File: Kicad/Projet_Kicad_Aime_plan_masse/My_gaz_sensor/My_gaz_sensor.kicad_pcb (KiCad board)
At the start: 2 copper layers, 134.6 x 64.8 mm, 23 parts, among them J1 Conn_01x03, J2 Conn_01x03, P1 Power, P2 Analog, P3 Digital, P4 Digital, P5 CONN_01X01, P6 CONN_01X01, P7 CONN_01X01, P8 CONN_01X01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

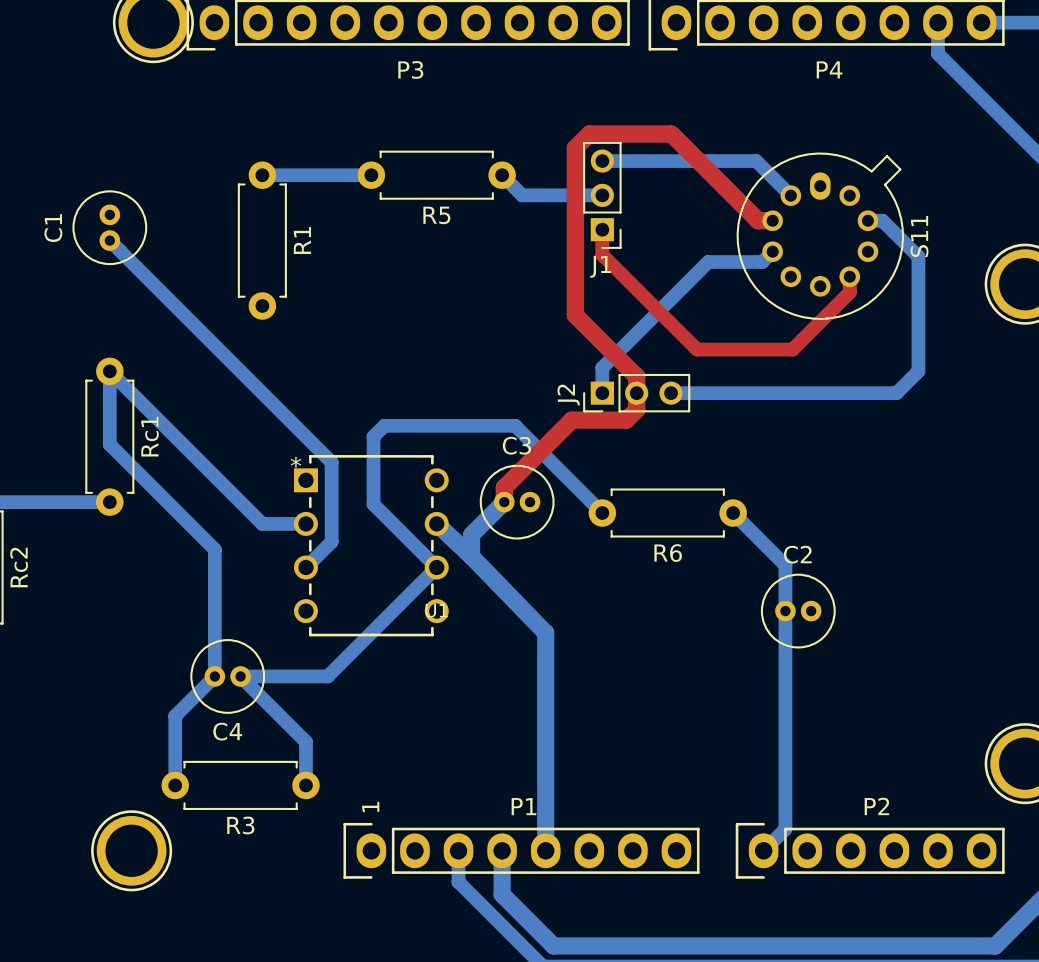
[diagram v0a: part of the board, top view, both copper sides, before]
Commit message: Refactor valeur C4
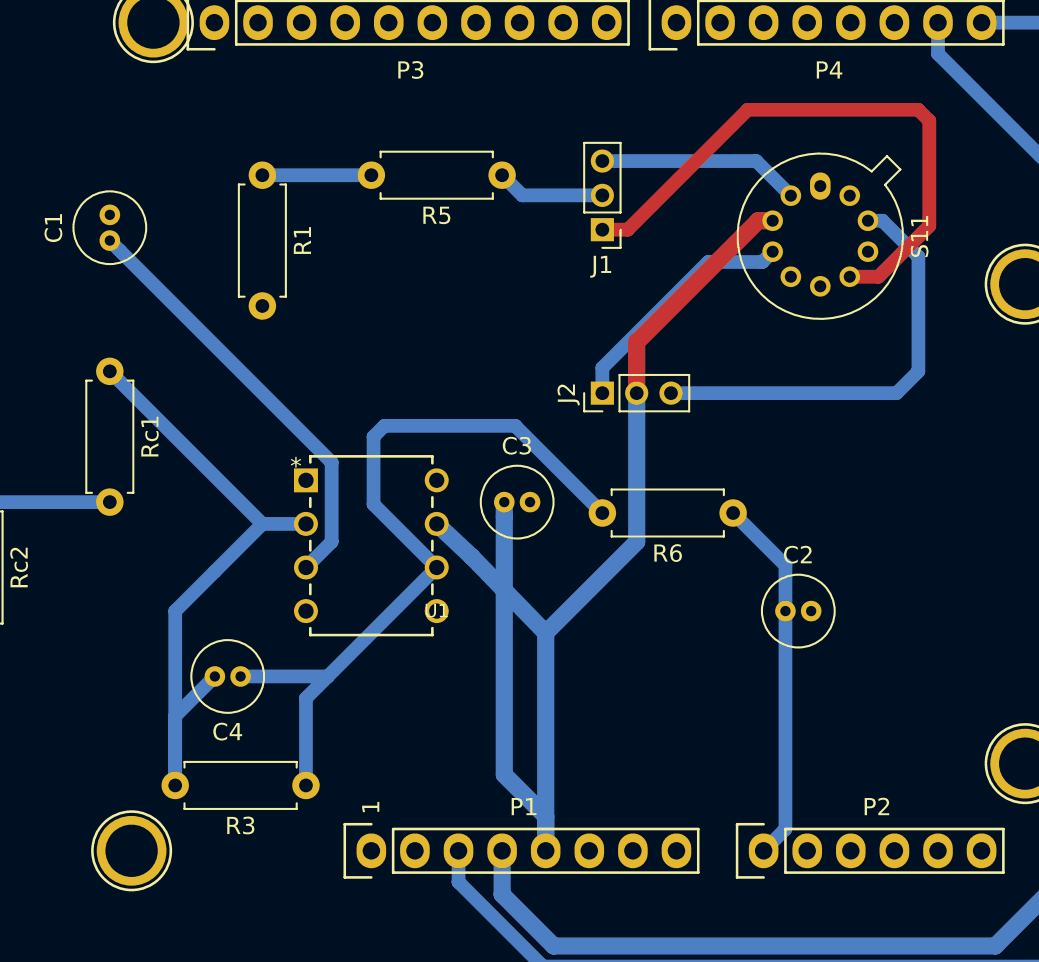
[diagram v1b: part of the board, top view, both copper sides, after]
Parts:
- C4: value 100n -> 1µ
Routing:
- net /GazSensorRight1: track 20.5 -> 34.2 mm
- net +5V: track 66.7 -> 73.0 mm
- net Net-(C4-Pad2): track 42.7 -> 39.8 mm
- net Net-(C4-Pad1): track 46.8 -> 45.8 mm
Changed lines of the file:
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@@
     (thickness 1.6)
     (drawings 25)
-    (tracks 90)
+    (tracks 84)
     (zones 0)
     (modules 23)
@@
       (effects (font (size 1 1) (thickness 0.15)))
     )
-    (fp_text value 100n (at 0.75 3.25) (layer F.Fab)
+    (fp_text value 1µ (at 0.75 3.25) (layer F.Fab)
       (effects (font (size 1 1) (thickness 0.15)))
     )
@@
   (segment (start 135.128 107.315) (end 136.626501 105.816499) (width 0.8) (layer B.Cu) (net 31))
   (segment (start 138.938 84.455) (end 132.588 84.455) (width 0.8) (layer B.Cu) (net 31))
-  (segment (start 135.128 120.015) (end 135.128 117.475) (width 0.8) (layer B.Cu) (net 32))
-  (segment (start 135.128 117.475) (end 131.318 113.665) (width 0.8) (layer B.Cu) (net 32))
   (segment (start 136.398 113.665) (end 142.748 107.315) (width 0.8) (layer B.Cu) (net 32))
   (segment (start 131.318 113.665) (end 136.398 113.665) (width 0.8) (layer B.Cu) (net 32))
@@
   (segment (start 139.7 99.06) (end 139.065 99.695) (width 0.8) (layer B.Cu) (net 32))
   (segment (start 147.32 99.06) (end 139.7 99.06) (width 0.8) (layer B.Cu) (net 32))
+  (segment (start 135.128 114.935) (end 136.398 113.665) (width 0.8) (layer B.Cu) (net 32))
+  (segment (start 135.128 120.015) (end 135.128 114.935) (width 0.8) (layer B.Cu) (net 32))
   (segment (start 132.588 104.775) (end 123.698 95.885) (width 0.8) (layer B.Cu) (net 33))
   (segment (start 135.128 104.775) (end 132.588 104.775) (width 0.8) (layer B.Cu) (net 33))
+  (segment (start 129.818 107.545) (end 132.588 104.775) (width 0.8) (layer B.Cu) (net 33))
+  (segment (start 127.508 109.855) (end 129.818 107.545) (width 0.8) (layer B.Cu) (net 33))
+  (segment (start 127.508 120.015) (end 127.508 109.855) (width 0.8) (layer B.Cu) (net 33))
   (segment (start 127.508 115.975) (end 129.818 113.665) (width 0.8) (layer B.Cu) (net 33))
   (segment (start 127.508 120.015) (end 127.508 115.975) (width 0.8) (layer B.Cu) (net 33))
-  (segment (start 129.818 113.665) (end 129.818 106.275) (width 0.8) (layer B.Cu) (net 33))
-  (segment (start 123.698 100.155) (end 123.698 95.885) (width 0.8) (layer B.Cu) (net 33))
-  (segment (start 129.818 106.275) (end 123.698 100.155) (width 0.8) (layer B.Cu) (net 33))
   (segment (start 116.078 103.505) (end 123.698 103.505) (width 0.8) (layer B.Cu) (net 36))
   (segment (start 149.098 123.825) (end 149.098 111.125) (width 1) (layer B.Cu) (net 44))
   (segment (start 149.098 111.125) (end 144.78 106.68) (width 1) (layer B.Cu) (net 44))
   (segment (start 144.78 106.68) (end 142.748 104.775) (width 1) (layer B.Cu) (net 44))
-  (segment (start 144.78 105.41) (end 146.685 103.505) (width 1) (layer B.Cu) (net 44))
-  (segment (start 144.78 106.68) (end 144.78 105.41) (width 1) (layer B.Cu) (net 44))
-  (segment (start 154.4 98.109594) (end 154.4 97.155) (width 1) (layer F.Cu) (net 44))
-  (segment (start 153.795001 98.730001) (end 154.4 98.125002) (width 1) (layer F.Cu) (net 44))
-  (segment (start 150.611471 98.730001) (end 153.795001 98.730001) (width 1) (layer F.Cu) (net 44))
-  (segment (start 146.685 102.656472) (end 150.611471 98.730001) (width 1) (layer F.Cu) (net 44))
-  (segment (start 154.4 98.125002) (end 154.4 98.109594) (width 1) (layer F.Cu) (net 44))
-  (segment (start 146.685 103.505) (end 146.685 102.656472) (width 1) (layer F.Cu) (net 44))
-  (segment (start 154.4 96.184998) (end 154.4 96.200406) (width 1) (layer F.Cu) (net 44))
-  (segment (start 150.824999 92.609997) (end 154.4 96.184998) (width 1) (layer F.Cu) (net 44))
-  (segment (start 151.643999 82.054999) (end 150.824999 82.873999) (width 1) (layer F.Cu) (net 44))
-  (segment (start 156.421716 82.054999) (end 151.643999 82.054999) (width 1) (layer F.Cu) (net 44))
-  (segment (start 150.824999 82.873999) (end 150.824999 92.609997) (width 1) (layer F.Cu) (net 44))
-  (segment (start 161.474387 87.10767) (end 156.421716 82.054999) (width 1) (layer F.Cu) (net 44))
-  (segment (start 154.4 96.200406) (end 154.4 97.155) (width 1) (layer F.Cu) (net 44))
-  (segment (start 162.322915 87.10767) (end 161.474387 87.10767) (width 1) (layer F.Cu) (net 44))
+  (segment (start 146.685 104.353528) (end 146.685 103.505) (width 1) (layer B.Cu) (net 44))
+  (segment (start 146.685 119.396) (end 146.685 104.353528) (width 1) (layer B.Cu) (net 44))
+  (segment (start 149.098 121.809) (end 146.685 119.396) (width 1) (layer B.Cu) (net 44))
+  (segment (start 149.098 123.825) (end 149.098 121.809) (width 1) (layer B.Cu) (net 44))
+  (segment (start 161.474387 87.10767) (end 162.322915 87.10767) (width 1) (layer F.Cu) (net 44))
+  (segment (start 154.4 97.155) (end 154.4 94.182057) (width 1) (layer F.Cu) (net 44))
+  (segment (start 154.4 94.182057) (end 161.474387 87.10767) (width 1) (layer F.Cu) (net 44))
+  (segment (start 154.4 105.823) (end 154.4 97.155) (width 1) (layer B.Cu) (net 44))
+  (segment (start 149.098 111.125) (end 154.4 105.823) (width 1) (layer B.Cu) (net 44))
   (segment (start 147.733 85.63) (end 146.558 84.455) (width 0.8) (layer B.Cu) (net 45))
   (segment (start 152.4 85.63) (end 147.733 85.63) (width 0.8) (layer B.Cu) (net 45))
@@
   (segment (start 169.545 97.155) (end 156.4 97.155) (width 0.8) (layer B.Cu) (net 46))
   (segment (start 170.815 95.885) (end 169.545 97.155) (width 0.8) (layer B.Cu) (net 46))
-  (segment (start 152.4 89.105) (end 157.91 94.615) (width 0.8) (layer F.Cu) (net 47))
-  (segment (start 152.4 87.63) (end 152.4 89.105) (width 0.8) (layer F.Cu) (net 47))
-  (segment (start 166.816333 91.220858) (end 166.816333 90.37233) (width 0.8) (layer F.Cu) (net 47))
-  (segment (start 166.816333 91.285669) (end 166.816333 91.220858) (width 0.8) (layer F.Cu) (net 47))
-  (segment (start 163.487002 94.615) (end 166.816333 91.285669) (width 0.8) (layer F.Cu) (net 47))
-  (segment (start 157.91 94.615) (end 163.487002 94.615) (width 0.8) (layer F.Cu) (net 47))
+  (segment (start 168.489087 90.37233) (end 171.45 87.411417) (width 0.8) (layer F.Cu) (net 47))
+  (segment (start 166.816333 90.37233) (end 168.489087 90.37233) (width 0.8) (layer F.Cu) (net 47))
+  (segment (start 171.45 87.411417) (end 171.45 81.28) (width 0.8) (layer F.Cu) (net 47))
+  (segment (start 171.45 81.28) (end 170.815 80.645) (width 0.8) (layer F.Cu) (net 47))
+  (segment (start 153.875 87.63) (end 152.4 87.63) (width 0.8) (layer F.Cu) (net 47))
+  (segment (start 160.86 80.645) (end 153.875 87.63) (width 0.8) (layer F.Cu) (net 47))
+  (segment (start 170.815 80.645) (end 160.86 80.645) (width 0.8) (layer F.Cu) (net 47))
   (segment (start 152.4 95.68) (end 152.4 97.155) (width 0.8) (layer B.Cu) (net 49))
   (segment (start 158.567671 89.512329) (end 152.4 95.68) (width 0.8) (layer B.Cu) (net 49))

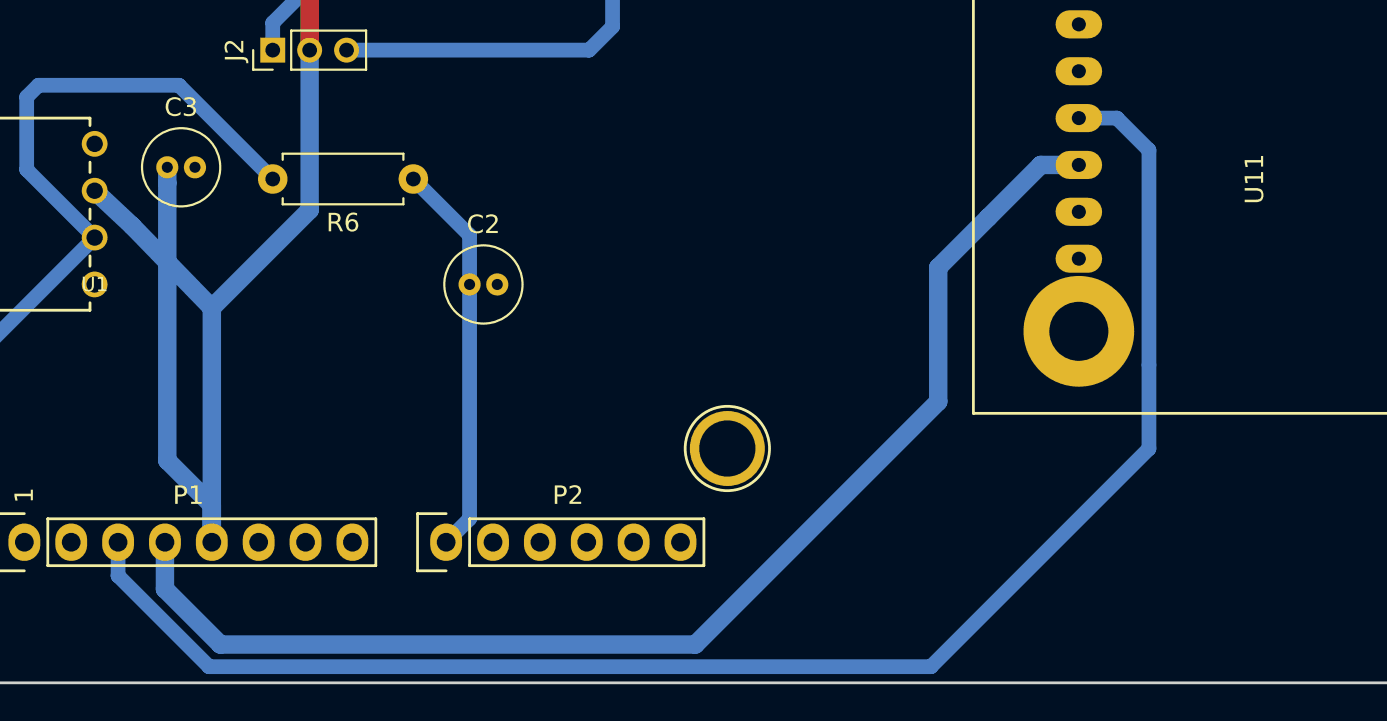
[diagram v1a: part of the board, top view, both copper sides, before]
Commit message: Reduction des near-to-pad
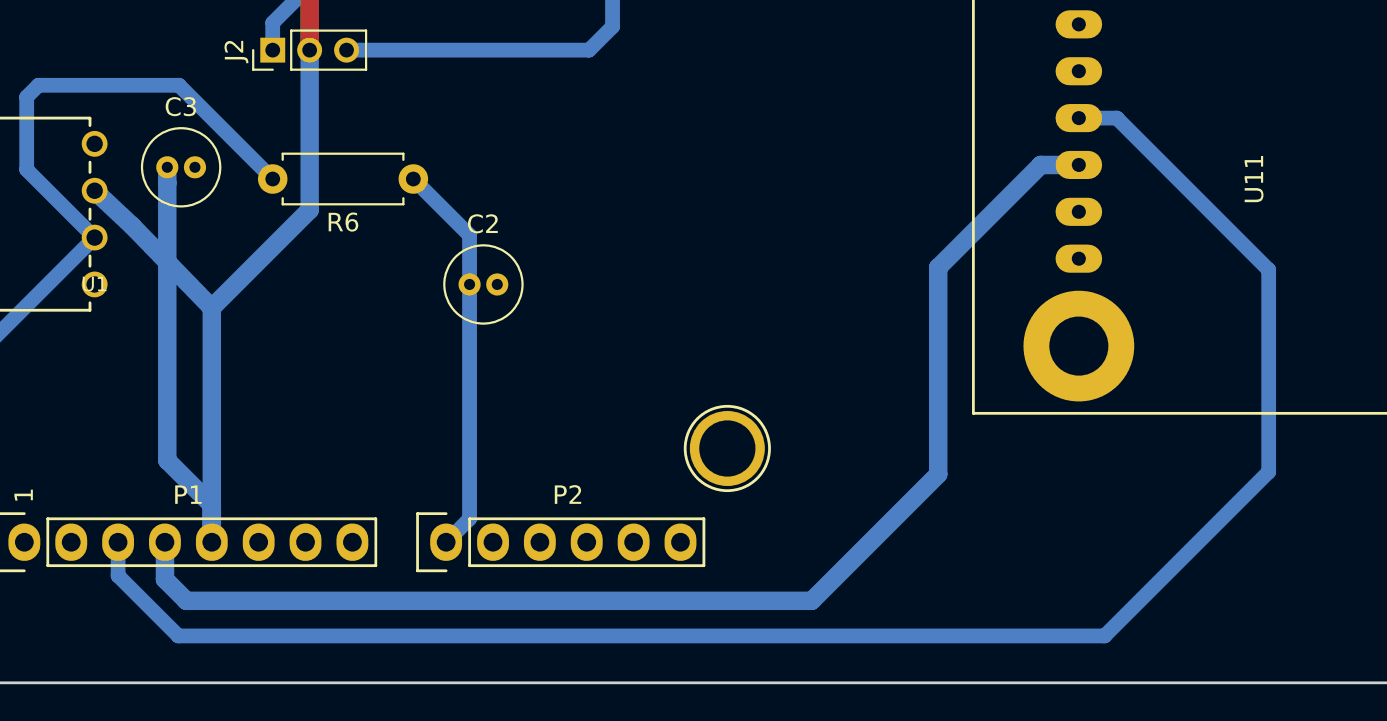
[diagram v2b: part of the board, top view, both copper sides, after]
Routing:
- net /Reset: track 85.3 -> 93.9 mm

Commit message: Changement pour s'adapter à la datasheet
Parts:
- added R7: R, Resistor_THT:R_Axial_DIN0207_L6.3mm_D2.5mm_P7.62mm_Horizontal, F.Cu at (170.8, 111.8)
- moved J2 33.8 mm to (186.1, 100.3), turned to 180 degrees
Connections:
- J2 pad 2: +5V -> +3V3
- P2 pad 2: /A1 -> SensorTemp
- S11 pad 3: +5V -> +12V
- S11 pad 6: Net-(S11-Pad6) -> SensorTemp
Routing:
- net SensorTemp: track 0.00 -> 37.9 mm
- net +5V: track 73.0 -> 43.0 mm
- net /GazSensorLeft2: track 14.2 -> 34.8 mm
- net +3V3: track 68.4 -> 78.7 mm
- net /GazSensorRight2: track 25.4 -> 22.6 mm

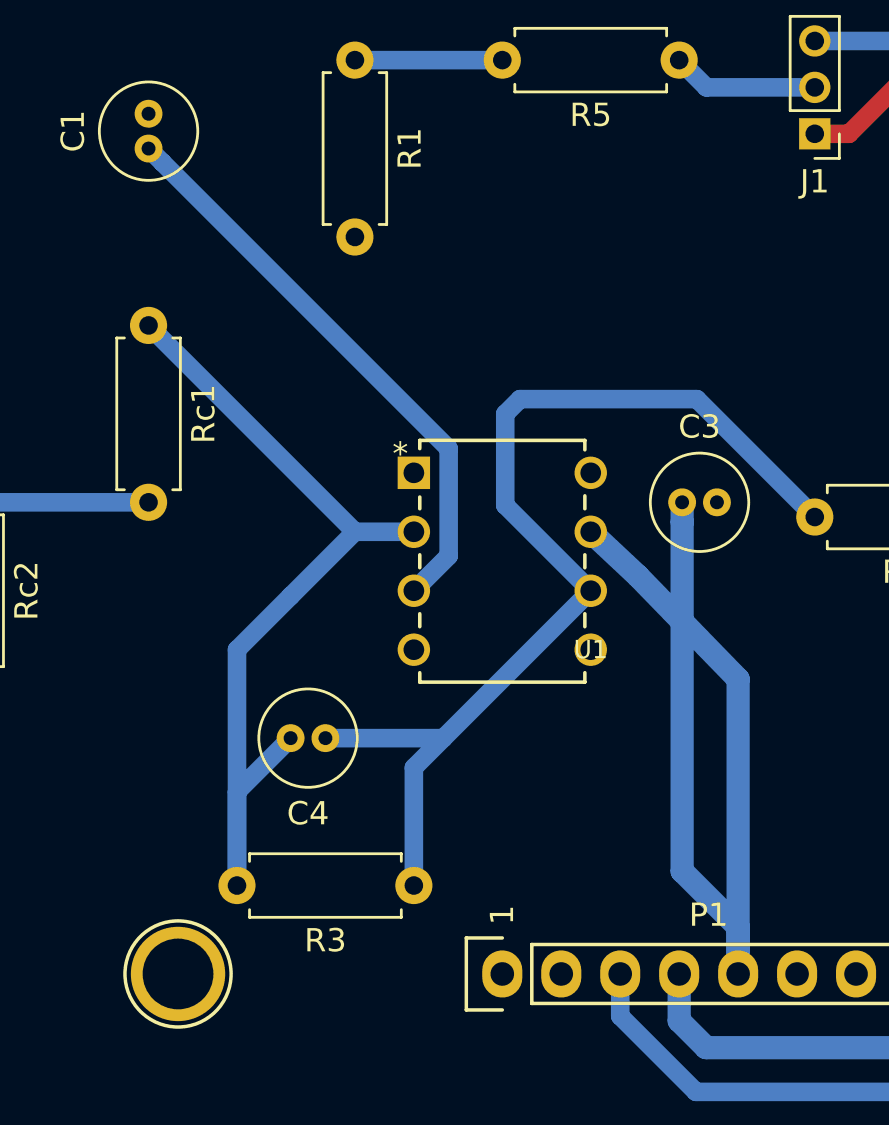
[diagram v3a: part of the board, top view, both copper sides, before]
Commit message: Refactor Aime Kicad Part
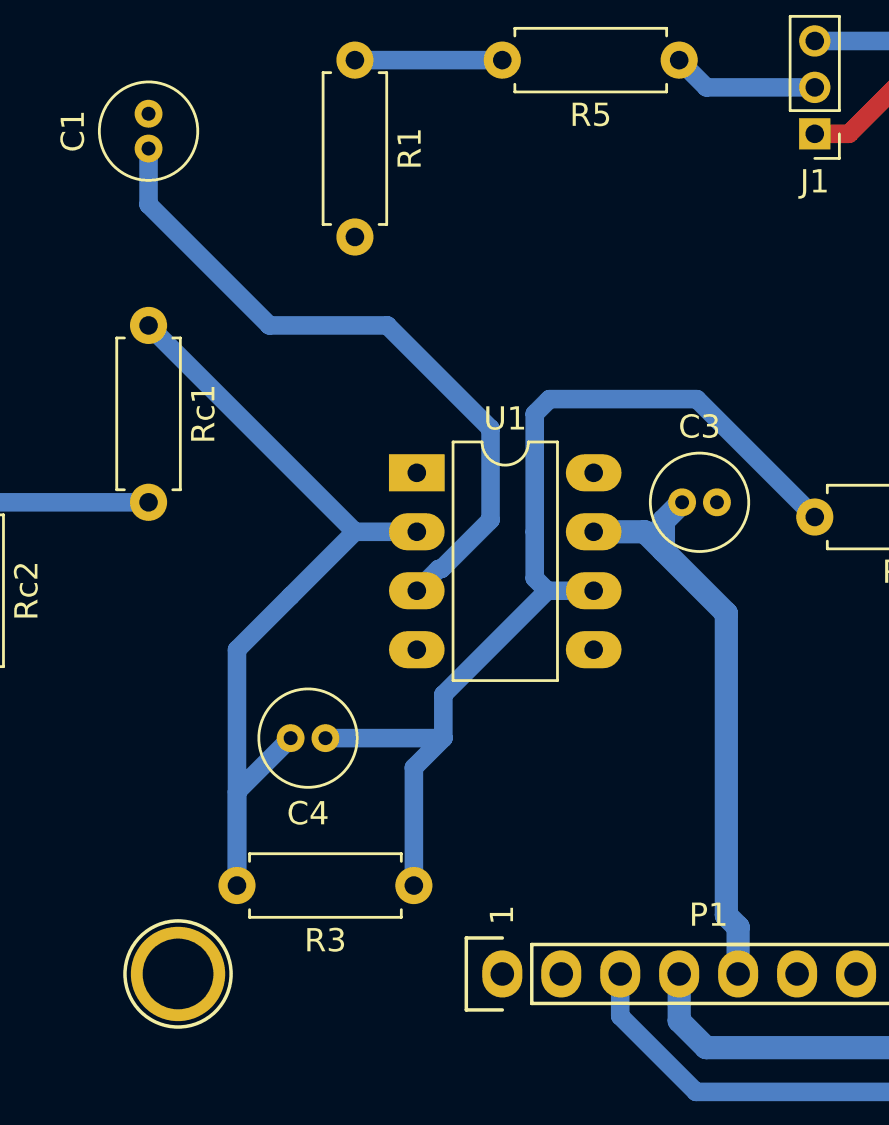
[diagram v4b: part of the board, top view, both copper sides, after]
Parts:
- U1: footprint MyComponent:PDIP-8_N -> Package_DIP:DIP-8_W7.62mm_LongPads
- moved U1 10.7 mm to (135.3, 102.2)
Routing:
- net +5V: track 43.0 -> 25.3 mm
- net Net-(C1-Pad1): track 31.4 -> 35.9 mm
- net Net-(C4-Pad1): track 45.8 -> 44.4 mm
